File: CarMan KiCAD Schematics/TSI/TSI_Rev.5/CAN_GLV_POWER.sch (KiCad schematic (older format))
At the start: 52 parts, among them J31 Cooling Jumper, K2 G5LE-1-E, K3 SFS2-DC24V, K4 SFS2-DC24V, Q11 TN2130K1-G, U14 Bottom Left, U15 Top Left, U17 Top Right, U2 Bottom Right, U20 TLP293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

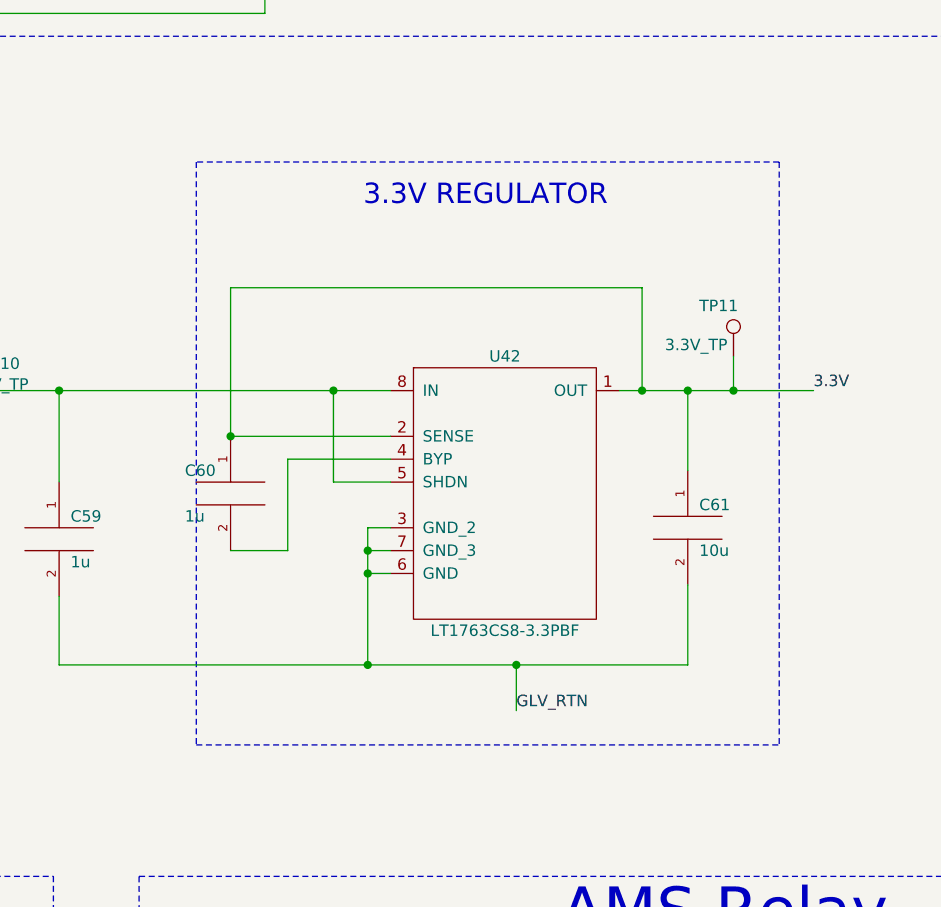
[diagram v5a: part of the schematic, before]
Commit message: Changed C60 from 1uF to 0.01uf
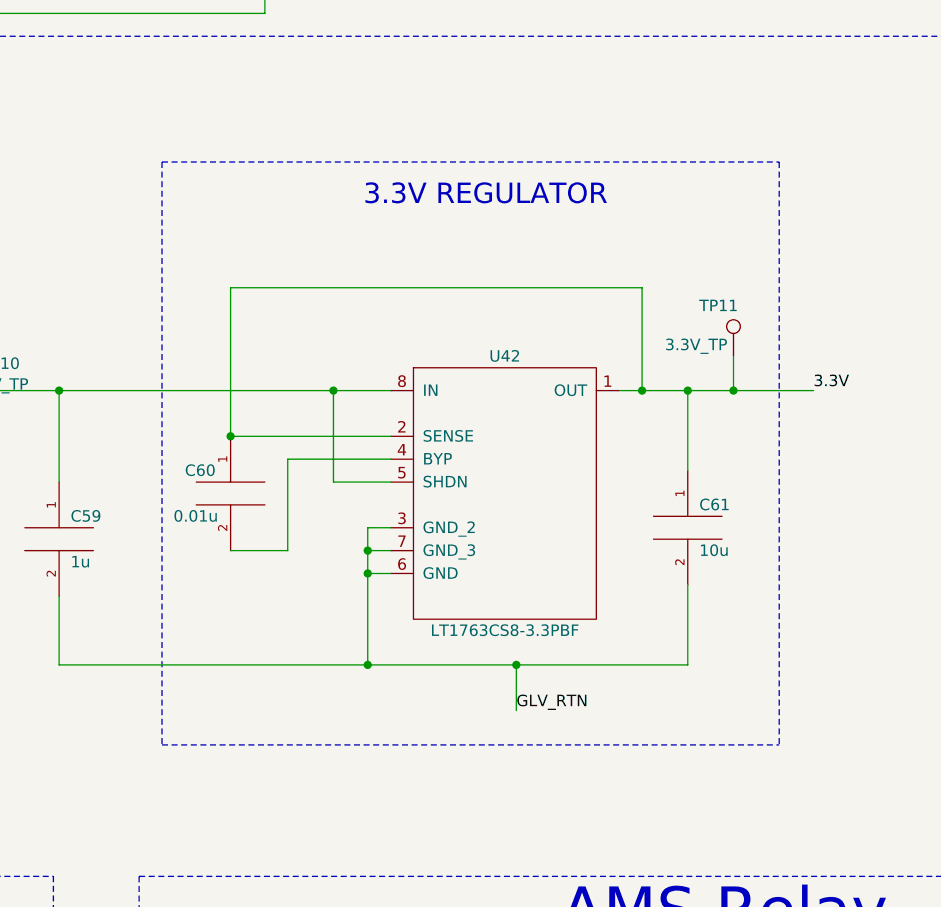
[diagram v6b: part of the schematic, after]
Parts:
- C60: value 1u -> 0.01u
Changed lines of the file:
@@
 P 6100 5250
 F 0 "C60" H 5900 5350 50  0000 L CNN
-F 1 "1u" H 5900 5150 50  0000 L CNN
+F 1 "0.01u" H 5850 5150 50  0000 L CNN
 F 2 "Capacitor_SMD:C_0805_2012Metric_Pad1.15x1.40mm_HandSolder" H 6100 5250 50  0001 C CNN
 F 3 "~" H 6100 5250 50  0001 C CNN
@@
 	5350 6000 6700 6000
 Wire Notes Line
-	5950 6350 8500 6350
-Wire Notes Line
-	8500 3800 5950 3800
-Wire Notes Line
 	8500 3800 8500 6350
-Wire Notes Line
-	5950 3800 5950 6350
 Text Notes 3750 4150 2    89   ~ 0
 DC/DC Converter\n
@@
 Text Notes 8850 7750 0    47   ~ 0
 15 mA through coil
+Wire Notes Line
+	5800 3800 8500 3800
+Wire Notes Line
+	5800 6350 8500 6350
+Wire Notes Line
+	5800 3800 5800 6350
 $EndSCHEMATC

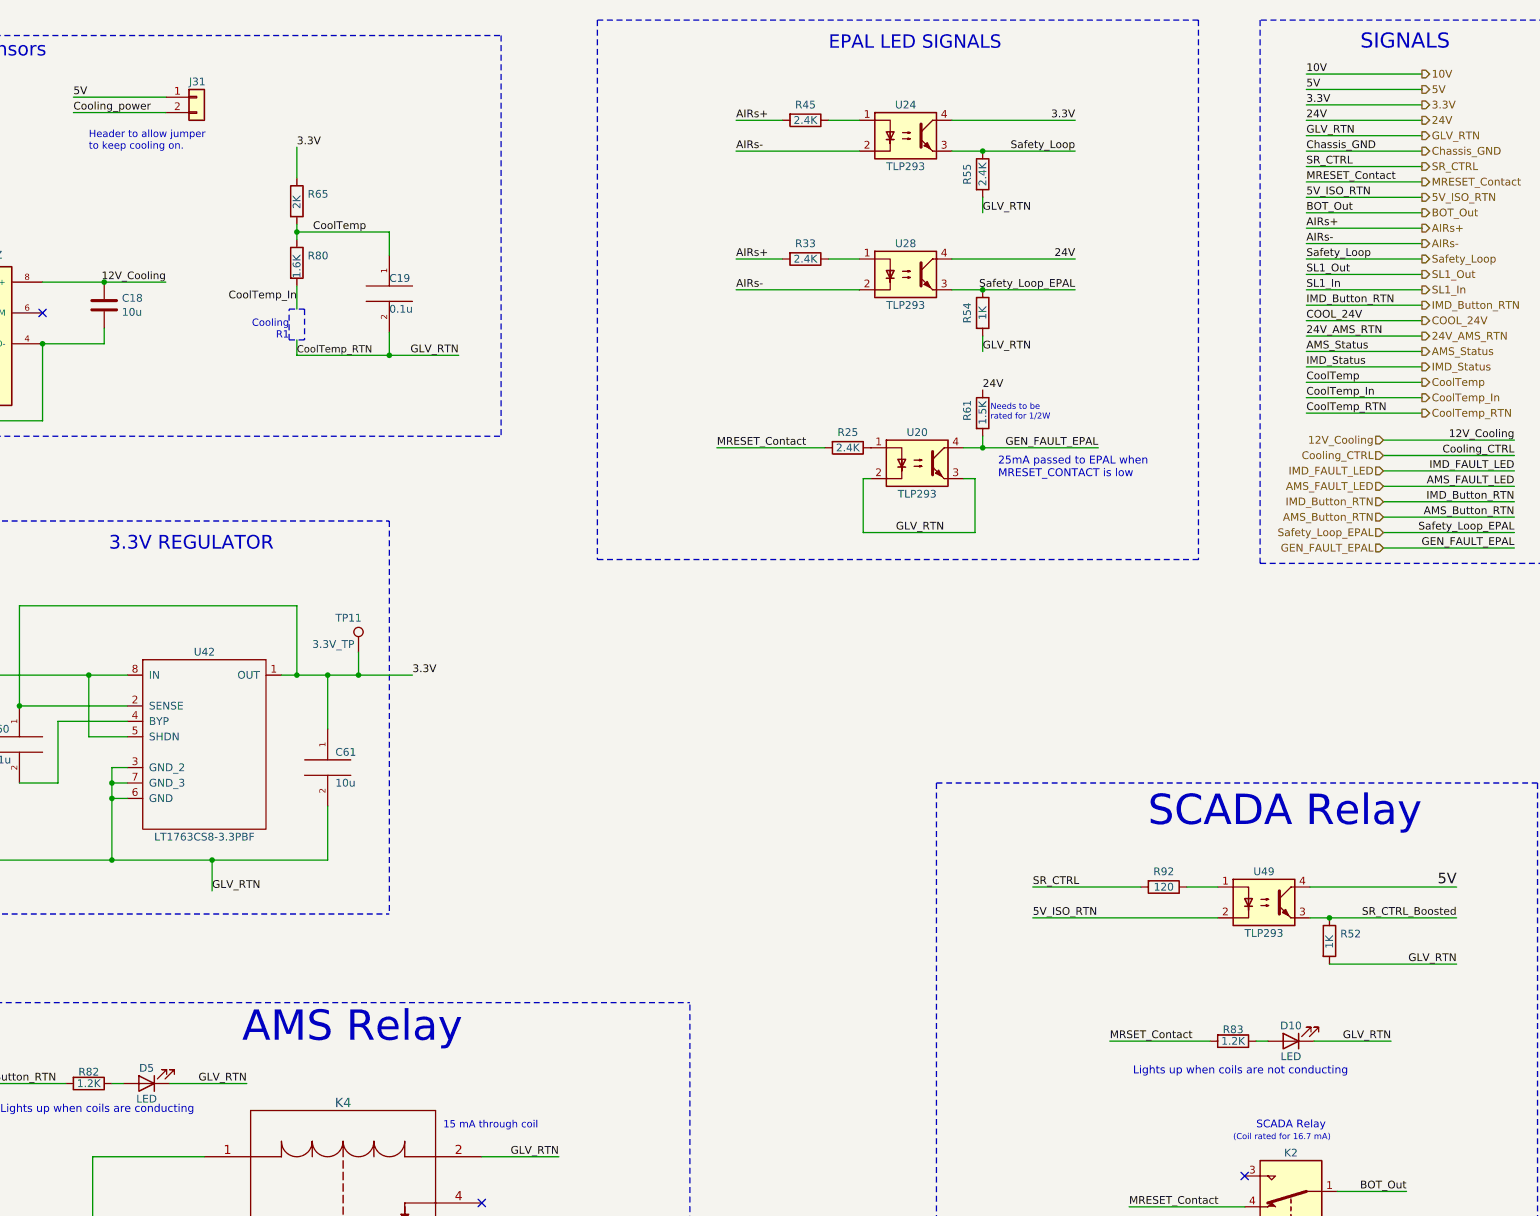
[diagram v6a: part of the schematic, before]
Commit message: Updated RTDS sound & added comments
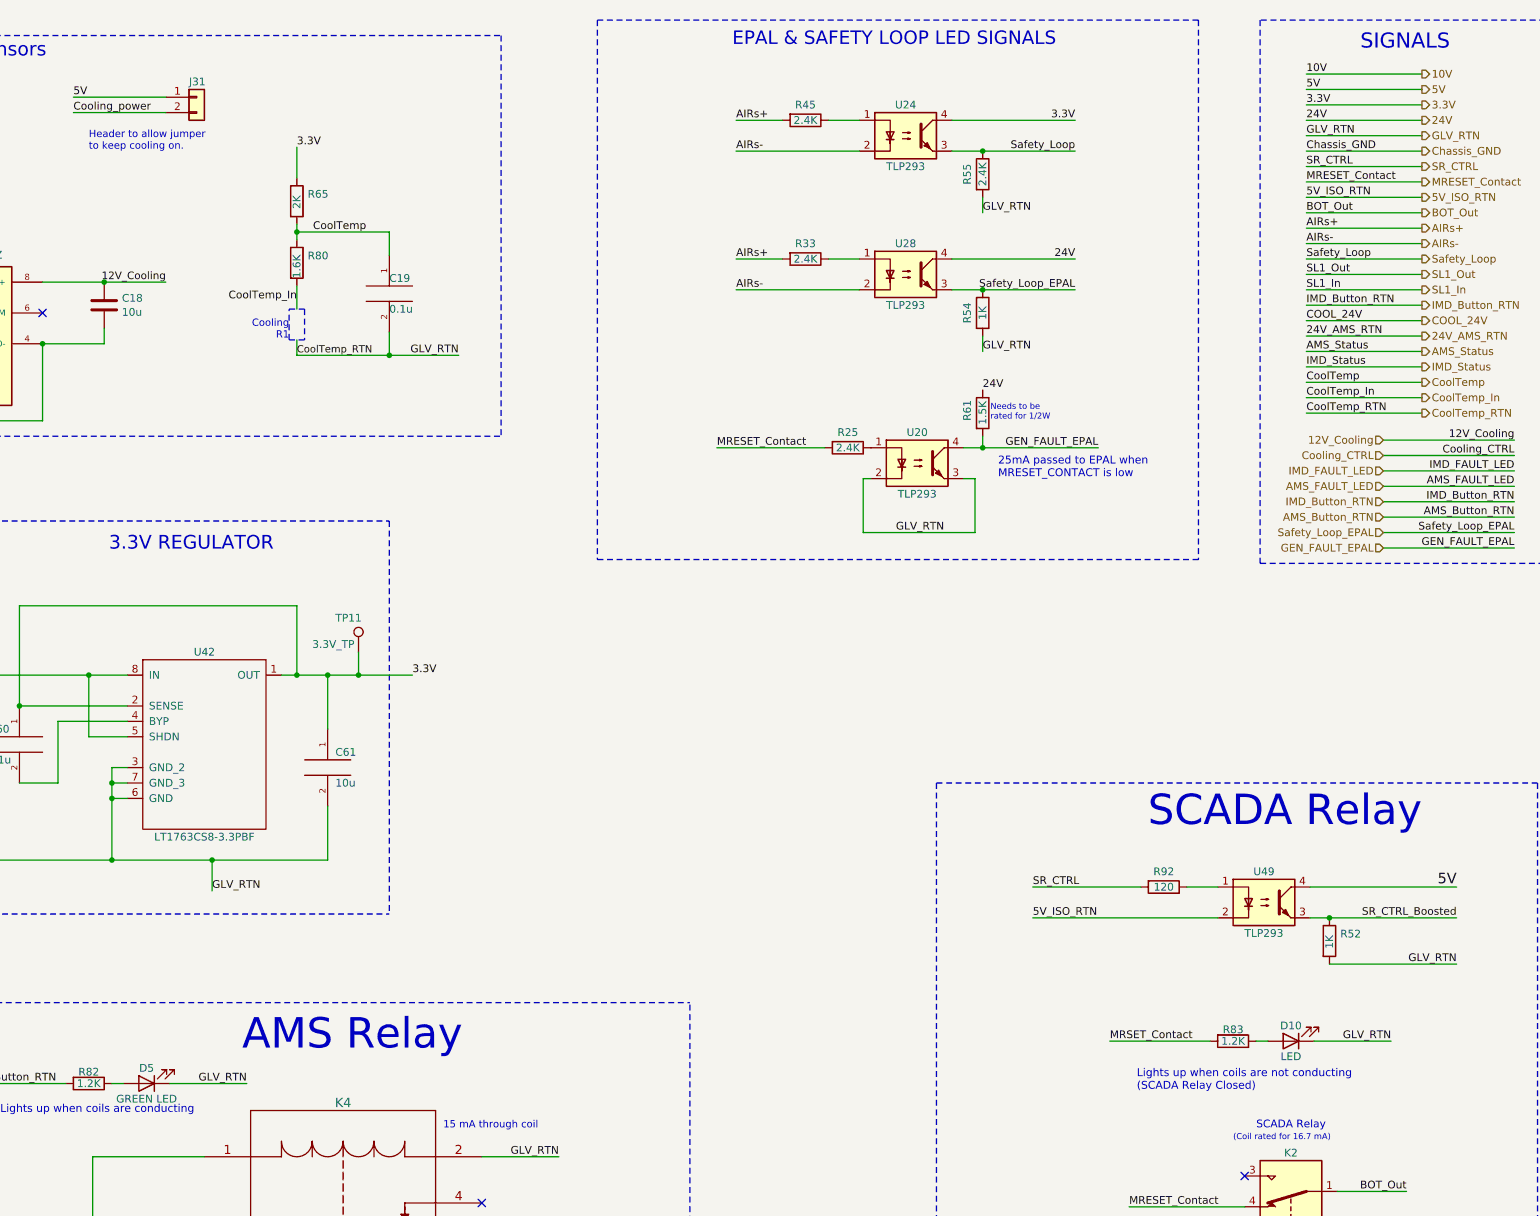
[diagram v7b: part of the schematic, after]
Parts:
- D5: value LED -> GREEN LED
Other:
- note added: "EPAL & SAFETY LOOP LED SIGNALS"
- note added: "Lights up when coils are not conducting\n(SCADA Relay Closed)"
- note removed: "EPAL LED SIGNALS"
- note removed: "Lights up when coils are not conducting"
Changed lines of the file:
@@
 Text Notes 3750 7225 2    197  ~ 0
 IMD Relay
-Text Notes 8975 7200 2    197  ~ 0
+Text Notes 8975 7250 2    197  ~ 0
 AMS Relay
 Text Label 4050 10775 2    50   ~ 0
@@
 Wire Notes Line
 	13750 550  9850 550
-Text Notes 11350 750  0    87   ~ 0
-EPAL LED SIGNALS
+Text Notes 10725 725  0    87   ~ 0
+EPAL & SAFETY LOOP LED SIGNALS
 Text Label 12950 1400 2    50   ~ 0
 Safety_Loop
@@
 P 6925 7450
 F 0 "D5" H 6925 7350 50  0000 C CNN
-F 1 "LED" H 6925 7550 50  0000 C CNN
+F 1 "GREEN LED" H 6925 7550 50  0000 C CNN
 F 2 "LED_SMD:LED_0805_2012Metric_Pad1.15x1.40mm_HandSolder" H 6925 7450 50  0001 C CNN
 F 3 "http://static.vcclite.com/pdf/VAOL-S8GT4-LED-0805-green.pdf" H 6925 7450 50  0001 C CNN
@@
 Wire Notes Line
 	14150 4075 16000 4075
-Text Notes 13325 7400 0    51   ~ 0
-Lights up when coils are not conducting
+Text Notes 13350 7500 0    51   ~ 0
+Lights up when coils are not conducting\n(SCADA Relay Closed)
 $Comp
 L Connector:TestPoint TP15
